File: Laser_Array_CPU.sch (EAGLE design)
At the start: 55 parts, among them IC1 PIC24FJ64GA004, J3 22-23-2021, M1 MOTOR, U2 MAX6817, U3 LP2985-28DBVTE4, U5 LP2985A-33DBVTE4, X1 22-23-2031, X4 22-23-2041, X5 22-23-2041, X6 22-23-2031

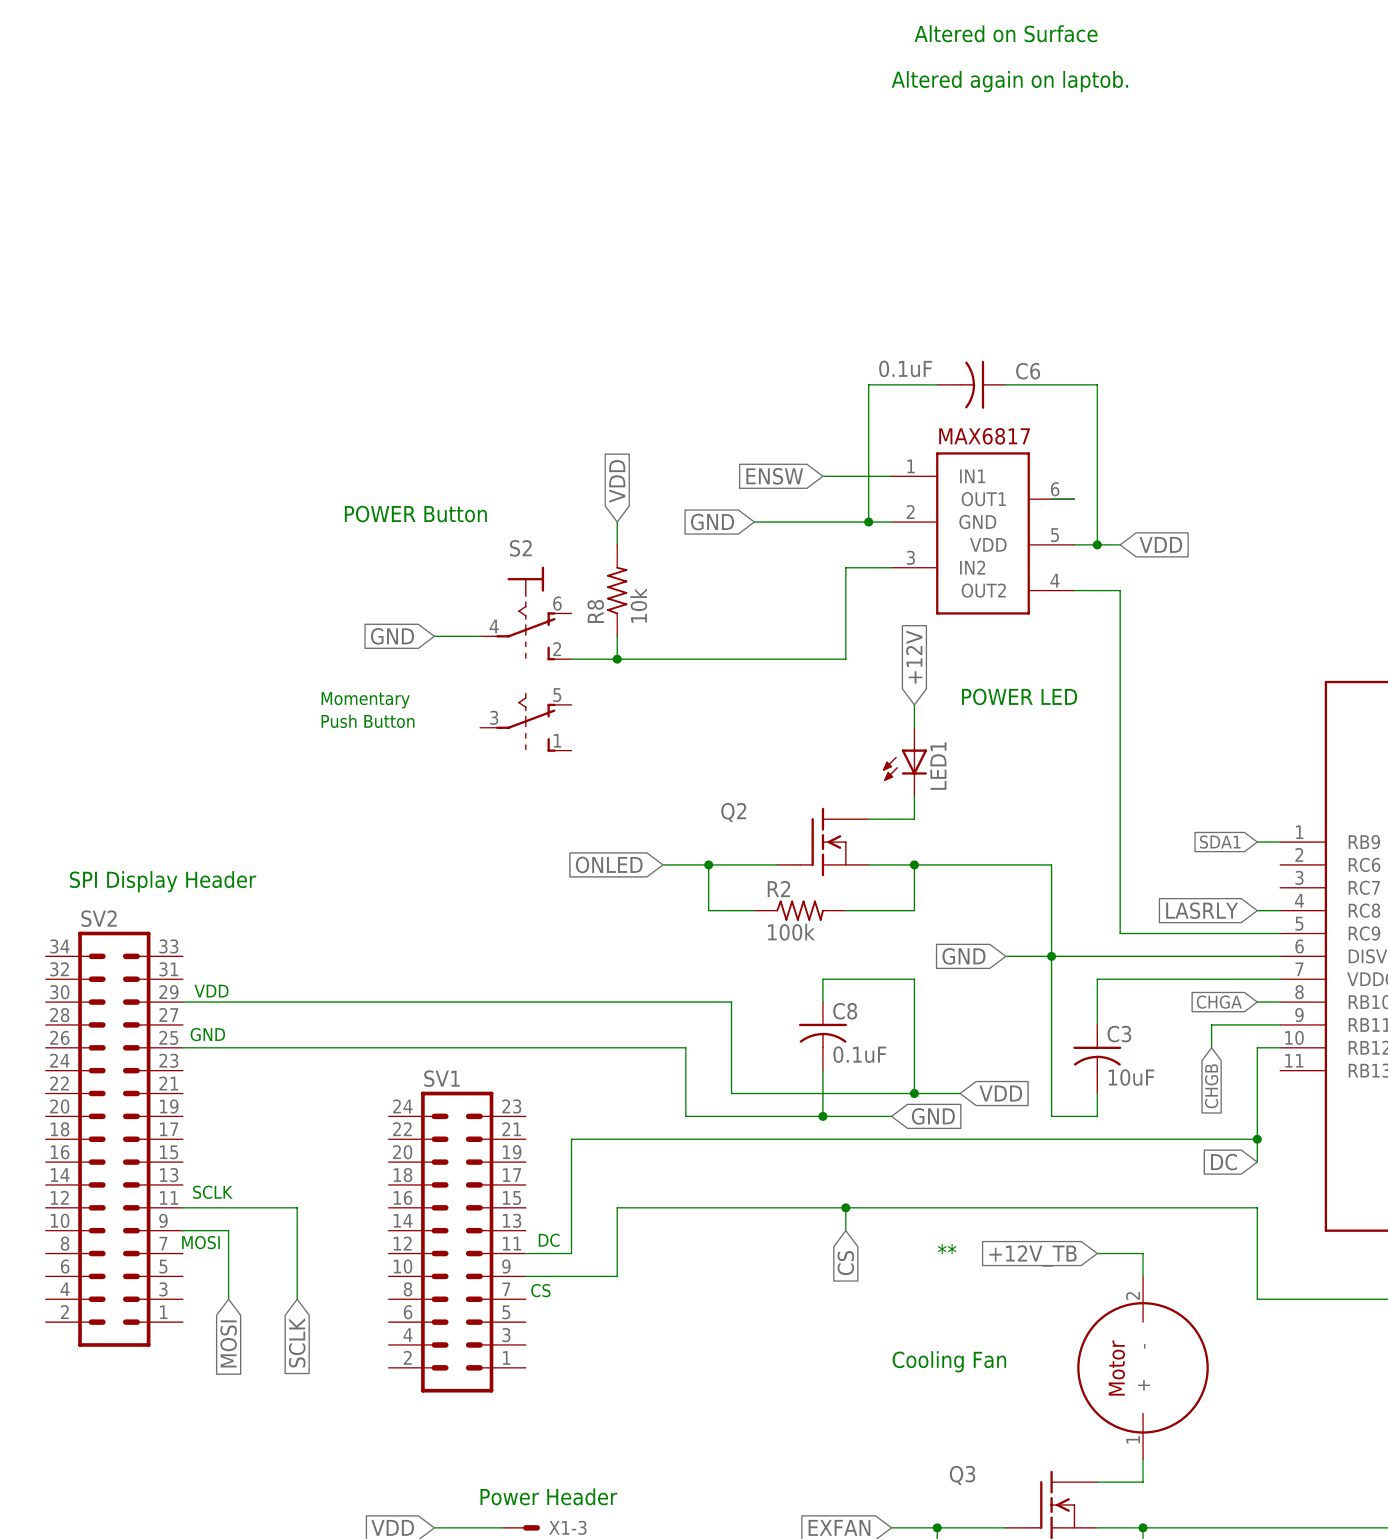
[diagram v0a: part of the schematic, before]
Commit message: Started CPU Board
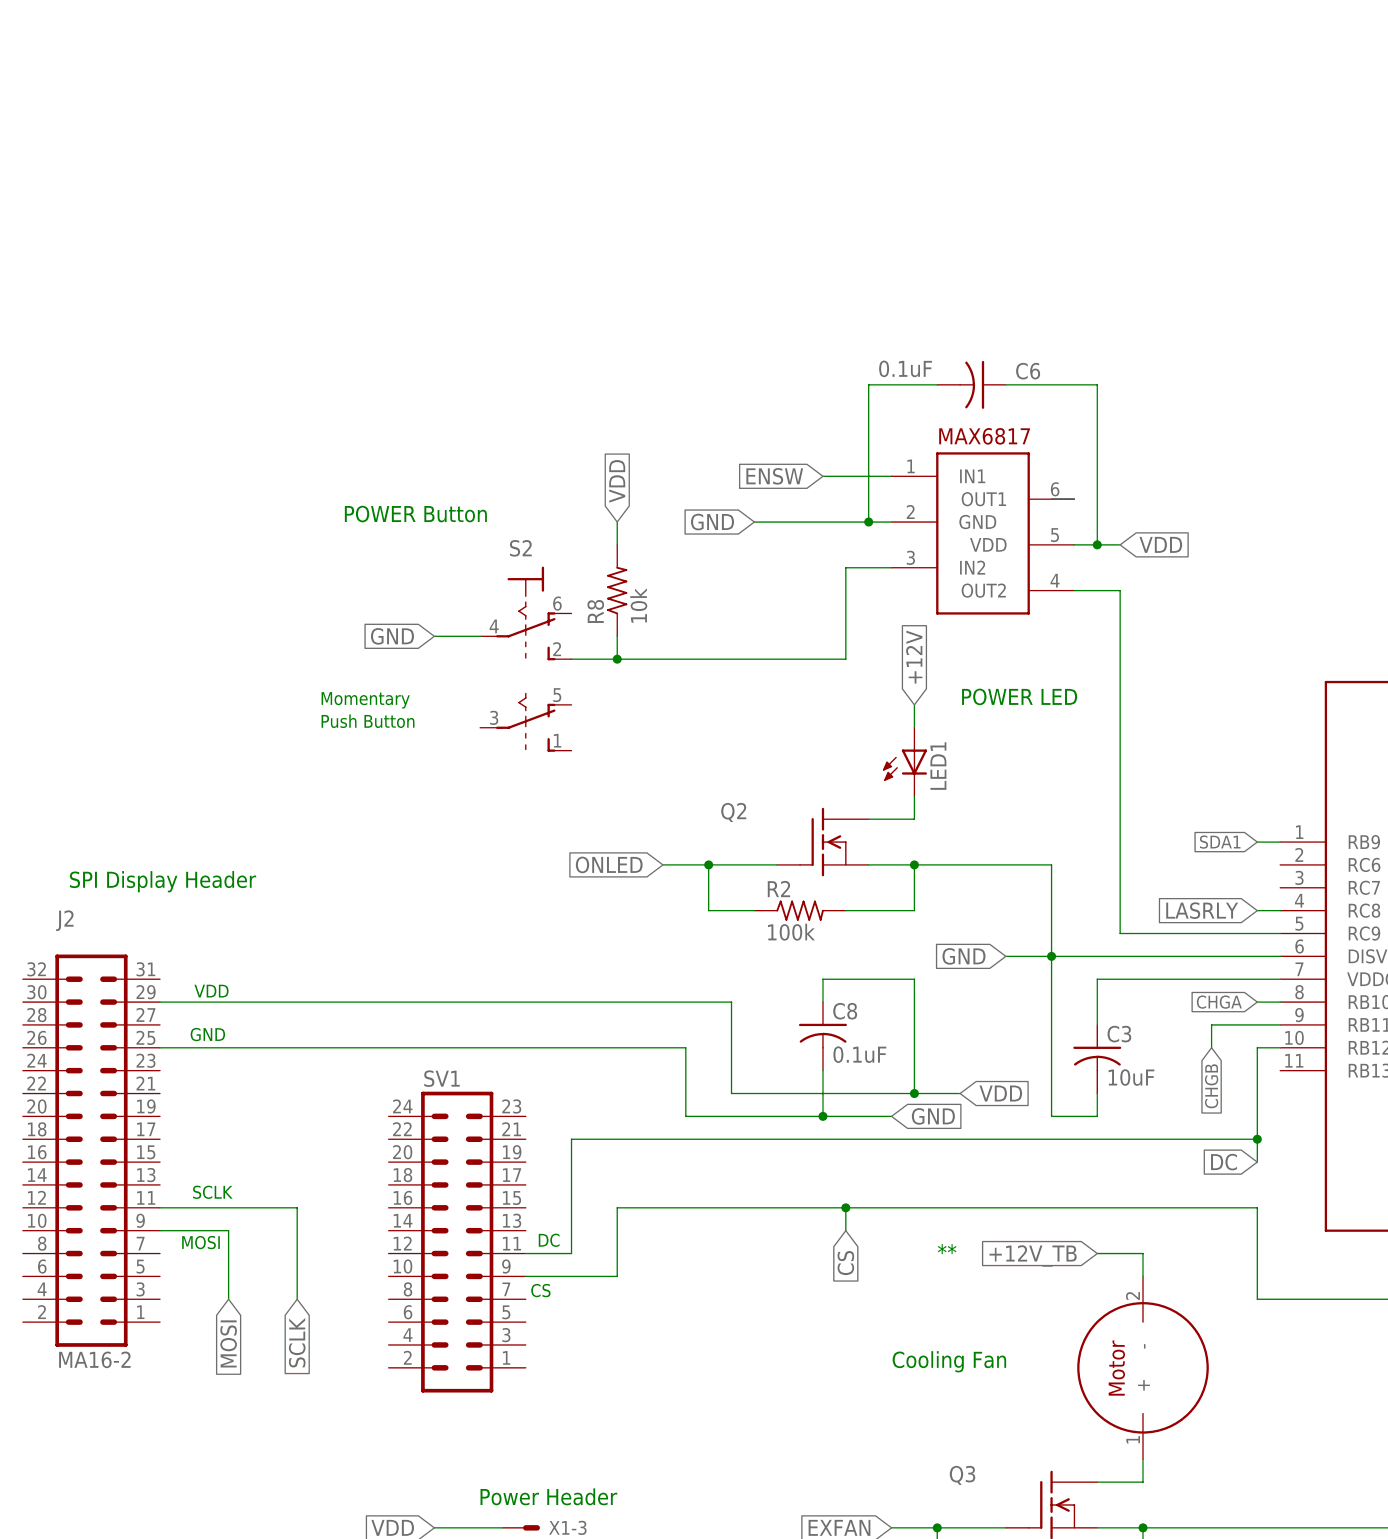
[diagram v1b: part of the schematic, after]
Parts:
- removed SV2: (no value), con-lstb:MA17-2W
- added J2: MA16-2, Mine:MA16-2
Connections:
- net GND: now also J2.25; no longer SV2.25
- net MOSI: now also J2.9; no longer SV2.9
- net SCLK: now also J2.11; no longer SV2.11
- net VDD: now also J2.29; no longer SV2.29
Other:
- note removed: "Altered again on laptob."
- note removed: "Altered on Surface"
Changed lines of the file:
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@@
 <part name="C17" library="rcl" deviceset="C-US" device="C0805" value="0.1uF"/>
 <part name="SV1" library="con-lstb" deviceset="MA12-2" device=""/>
-<part name="SV2" library="con-lstb" deviceset="MA17-2W" device=""/>
+<part name="J2" library="Mine" deviceset="MA16-2" device=""/>
 </parts>
 <sheets>
@@
 <text x="132.08" y="132.08" size="1.778" layer="91">Temp Sensor Breakout Board Header</text>
 <text x="86.36" y="104.14" size="1.778" layer="91">To Temp Sensor Breakout Board</text>
-<text x="-60.96" y="157.48" size="1.778" layer="91">Altered on Surface</text>
-<text x="-63.5" y="152.4" size="1.778" layer="91">Altered again on laptob.</text>
 </plain>
 <instances>
@@
 </instance>
 <instance part="SV1" gate="1" x="-111.76" y="22.86"/>
-<instance part="SV2" gate="1" x="-149.86" y="35.56"/>
+<instance part="J2" gate="G$1" x="-152.4" y="35.56"/>
 </instances>
 <busses>
@@
 <wire x1="-60.96" y1="53.34" x2="-60.96" y2="40.64" width="0.1524" layer="91"/>
 <junction x="-60.96" y="40.64"/>
-<pinref part="SV2" gate="1" pin="29"/>
-<wire x1="-142.24" y1="50.8" x2="-81.28" y2="50.8" width="0.1524" layer="91"/>
+<wire x1="-144.78" y1="50.8" x2="-81.28" y2="50.8" width="0.1524" layer="91"/>
 <wire x1="-81.28" y1="50.8" x2="-81.28" y2="40.64" width="0.1524" layer="91"/>
+<pinref part="J2" gate="G$1" pin="29"/>
 </segment>
 <segment>
@@
 <wire x1="-71.12" y1="38.1" x2="-86.36" y2="38.1" width="0.1524" layer="91"/>
 <wire x1="-86.36" y1="38.1" x2="-86.36" y2="45.72" width="0.1524" layer="91"/>
-<pinref part="SV2" gate="1" pin="25"/>
-<wire x1="-86.36" y1="45.72" x2="-142.24" y2="45.72" width="0.1524" layer="91"/>
+<wire x1="-86.36" y1="45.72" x2="-144.78" y2="45.72" width="0.1524" layer="91"/>
+<pinref part="J2" gate="G$1" pin="25"/>
 </segment>
 <segment>
@@
 </segment>
 <segment>
-<pinref part="SV2" gate="1" pin="11"/>
-<wire x1="-142.24" y1="27.94" x2="-129.54" y2="27.94" width="0.1524" layer="91"/>
+<wire x1="-144.78" y1="27.94" x2="-129.54" y2="27.94" width="0.1524" layer="91"/>
 <wire x1="-129.54" y1="27.94" x2="-129.54" y2="17.78" width="0.1524" layer="91"/>
 <label x="-129.54" y="17.78" size="1.778" layer="95" rot="R270" xref="yes"/>
+<pinref part="J2" gate="G$1" pin="11"/>
 </segment>
 </net>
@@
 </segment>
 <segment>
-<pinref part="SV2" gate="1" pin="9"/>
-<wire x1="-142.24" y1="25.4" x2="-137.16" y2="25.4" width="0.1524" layer="91"/>
+<wire x1="-144.78" y1="25.4" x2="-137.16" y2="25.4" width="0.1524" layer="91"/>
 <wire x1="-137.16" y1="25.4" x2="-137.16" y2="17.78" width="0.1524" layer="91"/>
 <label x="-137.16" y="17.78" size="1.778" layer="95" rot="R270" xref="yes"/>
-</segment>
-</net>
+<pinref part="J2" gate="G$1" pin="9"/>
+</segment>
+</net>

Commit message: temperture sensor board & CPU board complete
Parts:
- removed J2: MA16-2, Mine:MA16-2
- removed LED1, LED26: (no value), Mine:LEDA5MM
- removed M1: MOTOR, Mine:MOTOR
- removed RLY1: RELAY_SPST, Mine:RELAY_SPST
- removed U5: LP2985A-33DBVTE4, Texas Instruments_By_element14_Batch_1:LP2985A-33DBVTE4
- removed X4: 22-23-2041, Mine:22-23-2041
- added C19: 470uF, rcl:CPOL-USF
- added C20, C21: 10nF, rcl:C-USC0805
- added D3, D4: 641-1014-6-ND, adafruit:DIODESOD-123
- added D5: S10M-TPMSCT_ND, Mine:S10M-TPMSCT_ND
- added D7, D8: LL4148FSCT-ND, semicon-smd-ipc:D-SOD-80
- added J4, J8, J9: 22-23-2021, Mine:22-23-2021
- added J6: (no value), Mine:RJ_25
- added Q5: (no value), Mine:QS5U34CT-ND_MOSFET_N_CHANNEL
- added R11: 200k, rcl:R-TRIMM3224X
- added R12: 10k, rcl:R-US_M0805
- added R15: 4.7k, rcl:R-US_M0805
- added R16: 10k, rcl:R-US_R0805
- added U1: MAX6817, Mine:MAX6817
- added X2, X3: 22-23-2041, Mine:22-23-2041
- C10: value 10nF -> 0.1uF
- C11, C9: value 10nF -> 18pF
- C12: value 10nF -> 1uF
- C13, C18: value 2.2uF -> 10nF
- C16: value 1uF -> 2.2uF
- C17: value 0.1uF -> 2.2uF
- C2: value 0.1uF -> 10F; device rcl:C-USC0805 -> rcl:CPOL-USE5-10.5
- C3: value 10uF -> 10F; device rcl:C-USC0805 -> rcl:CPOL-USE5-10.5
- C4: value 18pF -> 0.1uF
- C5: value 18pF -> 10uF
- C7: value 10uF -> 0.1uF; device Mine:CAP3X3 -> rcl:C-USC0805
- C8: value 0.1uF -> 10uF; device rcl:C-USC0805 -> Mine:CAP3X3
- D1: value LL4148FSCT-ND -> S10M-TPMSCT_ND; device semicon-smd-ipc:D-SOD-80 -> Mine:S10M-TPMSCT_ND
- D2: value LL4148FSCT-ND -> 641-1014-6-ND; device semicon-smd-ipc:D-SOD-80 -> adafruit:DIODESOD-123
- J1: value (none) -> MA16-2; device Mine:RJ_25 -> Mine:MA16-2
- Q1: device adafruit:CRYSTALSM49 -> Mine:QS5U34CT-ND_MOSFET_N_CHANNEL
- Q4: device Mine:QS5U34CT-ND_MOSFET_N_CHANNEL -> adafruit:CRYSTALSM49
- R10: value 330 -> 220k; device rcl:R-US_R0805 -> rcl:R-US_M0805
- R13: value 4.7k -> 10k
- R14: value 4.7k -> 100k; device rcl:R-US_M0805 -> rcl:R-US_R0805
- R3: value 100k -> 10R, 5W; device rcl:R-US_R0805 -> Mine:RESISTOR5W
- R4: value 220k -> 100k; device rcl:R-US_M0805 -> rcl:R-US_R0805
- R5: value 200k -> 10k; device rcl:R-TRIMM3224X -> rcl:R-US_R0805
- R6, R7: value 10k -> 4.7k
- R8: value 10k -> 100k
- R9: value 100k -> 4.7k; device rcl:R-US_R0805 -> rcl:R-US_M0805
- S1: value TACT_PB -> (none); device Mine:TACT_PB -> Mine:DPDT_TOGGLE
- S2: value (none) -> TACT_PB; device Mine:DPDT_TOGGLE -> Mine:TACT_PB
- U2: value MAX6817 -> LP2985-28DBVTE4; device Mine:MAX6817 -> Texas Instruments_By_element14_Batch_1:LP2985-28DBVTE4
- U3: value LP2985-28DBVTE4 -> LP2985A-33DBVTE4; device Texas Instruments_By_element14_Batch_1:LP2985-28DBVTE4 -> Texas Instruments_By_element14_Batch_1:LP2985A-33DBVTE4
- X6: value 22-23-2031 -> 22-23-2041; device Mine:22-23-2031 -> Mine:22-23-2041
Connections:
- removed net +12V_TB: M1.-, RLY11.1
- removed net A0: X5-3.S
- removed net ENSW: U2.IN1, X4-4.S
- removed net LASOUT: LED26.A, RLY12.S
- removed net N$12: M1.+, Q3.D
- removed net N$13: R5.E
- removed net N$14: U2.OUT1
- removed net N$29: LED26.C, R10.2
- removed net N$3: J1.1
- removed net N$35 (its old number): C12.1, U5.BYPASS
- new net CHGOUTA: IC1.RC6, X1-1.S
- new net CHGOUTB: IC1.RC7, X1-2.S
- new net DISPWR: IC1.RB14, Q5.G, R14.1
- new net ENSW_I: R16.1, U1.IN1, X5-4.S
- new net ENSW_O: IC1.RB15, U1.OUT1
- new net N$16: J4-1.S, Q2.D
- new net N$33: D3.C, D4.A, R3.2
- new net N$34: J8-1.S, Q3.D
- new net N$36: C2.-, C3.+
- new net N$37: C2.+, D5.A, R3.1
- new net N$55: C13.1, U2.BYPASS
- new net N$8: C1.2, J1.25, Q5.D
- new net VLASER: D1.C, X2-4.S, X6-4.S
- net !RESET: now also X6-3.S; no longer X5-4.S
- net +12V: now also C12.1, J3-1.S, R10.2, U2.ON/OFF, U2.VIN, X2-2.S, X3-3.S; no longer C16.1, LED1.A, R4.2, U5.ON/OFF, U5.VIN, X1-2.S, X6-2.S
- net CHGA: now also J9-1.S; no longer J3-1.S
- net CHGB: now also J9-2.S; no longer J3-2.S
- net ENCDR_A: now also C20.1, R12.1, X5-3.S; no longer C11.1, R7.1, X4-3.S
- net ENCDR_B: now also C18.1, R13.1, X5-2.S; no longer C10.1, R6.1, X4-2.S
- net EXFAN: now also Q2.G, R4.1; no longer Q3.G, R3.1
- net GND: now also C18.2, C19.-, C20.2, C21.2, C3.-, C7.1, C8.-, D8.A, J4-2.S, J6.4, J8-2.S, Q1.S, Q5.S, R11.A, R14.2, R4.2, R8.2, S1.P, S2.1, U1.GND, X1-3.S, X2-3.S, X3-4.S, X5-1.S; no longer C1.1, C2.2, C3.2, C7.-, C8.2, D2.A, J1.4, J2.25, Q4.S, R10.1, R3.2, R5.A, R9.2, S1.1, S2.P, U5.GND, X1-1.S, X4-1.S, X6-1.S
- net LASRLY: now also Q3.G, R8.1; no longer Q4.G, R9.1
- net MOSI: now also J1.9; no longer J2.9
- net N$1: now also C8.+, J6.6, R5.2, S2.2; no longer C7.+, J1.6, R1.2, S1.2
- net N$10: now also U1.OUT2; no longer U2.OUT2
- net N$11: now also J3-2.S, Q1.D; no longer LED1.C, Q2.D
- net N$15: now also D1.A, D2.C; no longer Q4.D, RLY11.2
- net N$2: now also C5.1; no longer C3.1
- net N$4: now also J6.2; no longer J1.2
- net N$5: now also J6.3; no longer J1.3
- net N$6: now also C9.1, Q4.1; no longer C5.1, Q1.1
- net N$7: now also C11.1, Q4.2; no longer C4.1, Q1.2
- net N$9: now also R1.1, S1.S, U1.IN2; no longer R8.1, S2.S, U2.IN2
- net ONLED: now also Q1.G; no longer Q2.G
- net SCL1: now also R7.1; no longer R14.1
- net SCL2: now also R15.1, X6-1.S; no longer X5-1.S
- net SCLK: now also J1.11; no longer J2.11
- net SDA1: now also R6.1; no longer R13.1
- net SDA2: now also R9.1, X6-2.S; no longer X5-2.S
- net VDD: now also C1.1, C10.1, C4.1, C7.2, D4.C, D5.C, J1.29, J6.5, R1.2, R12.2, R15.2, R16.2, R5.1, R9.2, U1.VDD, X3-1.S; no longer C1.2, C17.1, C2.1, C8.1, J1.5, J2.29, R1.1, R14.2, R8.2, S3.VDD, U2.VDD, X1-3.S, X6-3.S
- net VDD_TB: now also D2.A, D3.A, X2-1.S; no longer RLY12.P
- net VIN1: now also C21.1, D7.A, D8.C, R10.1, R11.S; no longer C9.1, D1.A, D2.C, R4.1, R5.S
- net VRR: now also C16.1, D7.C, U2.VOUT; no longer C18.1, D1.C, U3.VOUT
- net VTS: now also C17.1, C19.+, S3.VDD, U3.VOUT, X3-2.S; no longer C13.1, U5.VOUT
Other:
- note added: "*** Across contact screws."
- note added: "+12V_TB"
- note added: "3.1V"
- note added: "4.4V"
- note added: "CHGOUTLEDA"
- note added: "CHGOUTLEDB"
- note added: "Ext Fan Header"
- note added: "Laser Relay Header"
- note added: "ON LED Header"
- note added: "VDD_TB"
- note added: "VLASER"
- note added: "VTS"
- note removed: "**"
- note removed: "A0"
- note removed: "Cooling Fan"
- note removed: "POWER LED"
- moved on the sheet: C1, C10, C11, C12, C13, C14, C15, C16, C17, C18, C4, C5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
